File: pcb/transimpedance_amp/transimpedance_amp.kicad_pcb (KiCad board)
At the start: 2 copper layers, 80 x 50 mm, 48 parts, among them P1 CONN_01X05, P2 CONN_01X05, P3 CONN_01X05, P4 CONN_01X05, P5 CONN_01X05, P6 CONN_01X05, P7 CONN_01X05, P8 CONN_01X05, U1 AD8616

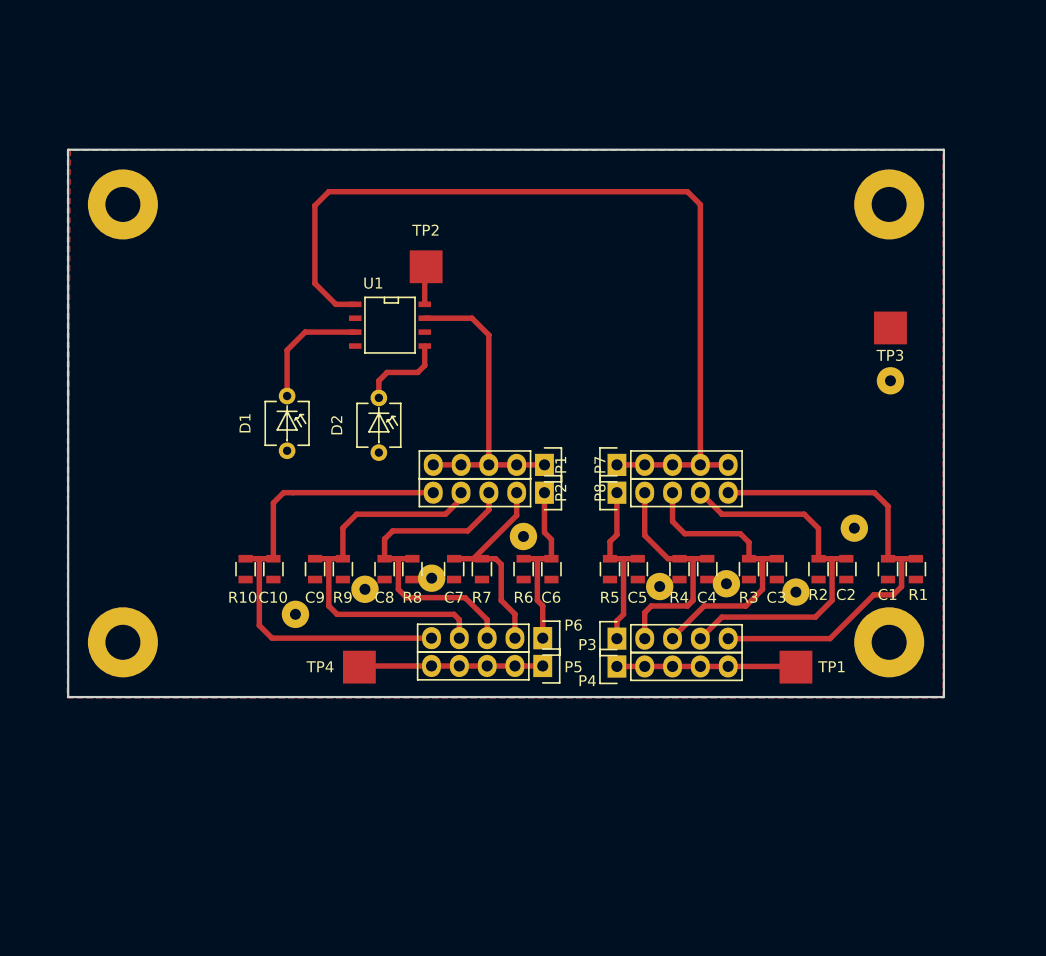
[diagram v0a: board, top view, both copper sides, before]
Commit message: Found a design error. Has to be corrected.
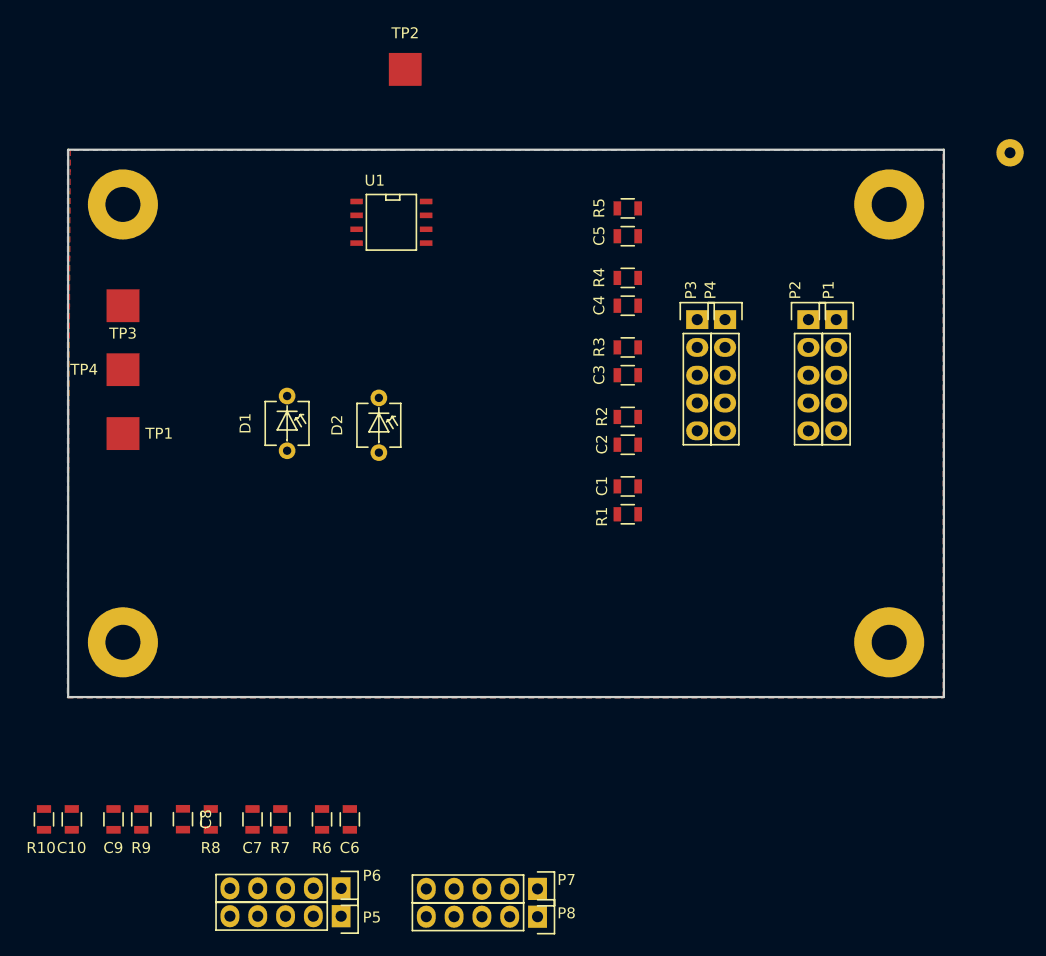
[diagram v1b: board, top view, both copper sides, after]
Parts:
- removed the REF** at (178.8, 115.6)
- removed the REF** at (167.1, 120.7)
- removed the REF** at (173.5, 121.4)
- removed the REF** at (161.0, 120.9)
- removed the REF** at (148.6, 116.3)
- removed the REF** at (140.2, 120.1)
- removed the REF** at (127.8, 123.4)
- removed the REF** at (134.1, 121.2)
- moved TP3 70.1 mm to (112.0, 95.2)
- moved TP1 65.1 mm to (112.0, 106.9)
- moved P7 38.7 mm to (149.9, 148.5)
- moved P8 38.7 mm to (149.9, 151.1)
- moved TP4 34.7 mm to (112.0, 101.1)
- moved P4 33.2 mm to (167.0, 96.5), turned to 0 degrees
- moved R5 33.0 mm to (158.1, 86.4), turned to 180 degrees
- moved C5 30.4 mm to (158.1, 88.9), turned to 180 degrees
- moved P3 30.1 mm to (164.5, 96.5), turned to 0 degrees
- moved C6 29.4 mm to (132.7, 142.2)
- moved C10 29.4 mm to (107.3, 142.2)
- moved C9 29.4 mm to (111.1, 142.2)
- moved C7 29.4 mm to (123.8, 142.2)
- moved P5 29.4 mm to (131.9, 151.0)
- moved R10 29.4 mm to (104.8, 142.2)
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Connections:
- C1 pad 2: GND -> Net-(C1-Pad2)
- C10 pad 2: GND -> Net-(C10-Pad2)
- C2 pad 2: GND -> Net-(C1-Pad2)
- C3 pad 2: GND -> Net-(C1-Pad2)
- C4 pad 2: GND -> Net-(C1-Pad2)
- C5 pad 2: GND -> Net-(C1-Pad2)
- C6 pad 2: GND -> Net-(C10-Pad2)
- C7 pad 2: GND -> Net-(C10-Pad2)
- C8 pad 2: GND -> Net-(C10-Pad2)
- C9 pad 2: GND -> Net-(C10-Pad2)
- D1 pad 1: Net-(D1-Pad1) -> Net-(C1-Pad2)
- D2 pad 1: Net-(D2-Pad1) -> Net-(C10-Pad2)
- R1 pad 2: GND -> Net-(C1-Pad2)
- R10 pad 2: GND -> Net-(C10-Pad2)
- R2 pad 2: GND -> Net-(C1-Pad2)
- R3 pad 2: GND -> Net-(C1-Pad2)
- R4 pad 2: GND -> Net-(C1-Pad2)
- R5 pad 2: GND -> Net-(C1-Pad2)
- R6 pad 2: GND -> Net-(C10-Pad2)
- R7 pad 2: GND -> Net-(C10-Pad2)
- R8 pad 2: GND -> Net-(C10-Pad2)
- R9 pad 2: GND -> Net-(C10-Pad2)
- U1 pad 3: Net-(D1-Pad1) -> Net-(C1-Pad2)
- U1 pad 5: Net-(D2-Pad1) -> Net-(C10-Pad2)
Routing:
- net Net-(P1-Pad1): track 81.7 -> 0.00 mm
- net Net-(C10-Pad1): track 44.9 -> 0.00 mm
- net Net-(C1-Pad1): track 42.8 -> 0.00 mm
- net Net-(C9-Pad1): track 36.3 -> 0.00 mm
- net Net-(C2-Pad1): track 35.1 -> 0.00 mm
- net Net-(C8-Pad1): track 30.5 -> 0.00 mm
- net Net-(P7-Pad1): track 28.5 -> 0.00 mm
- net Net-(C3-Pad1): track 27.5 -> 0.00 mm
- net Net-(C4-Pad1): track 21.6 -> 0.00 mm
- net Net-(C7-Pad1): track 20.2 -> 0.00 mm
- net Net-(C6-Pad1): track 17.0 -> 0.00 mm
- net Net-(P5-Pad1): track 16.8 -> 0.00 mm
- net Net-(C5-Pad1): track 16.4 -> 0.00 mm
- net Net-(P4-Pad1): track 16.4 -> 0.00 mm
- net Net-(D1-Pad1): track 11.1 -> 0.00 mm
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
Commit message: Finished layout. Sill room for optimization.
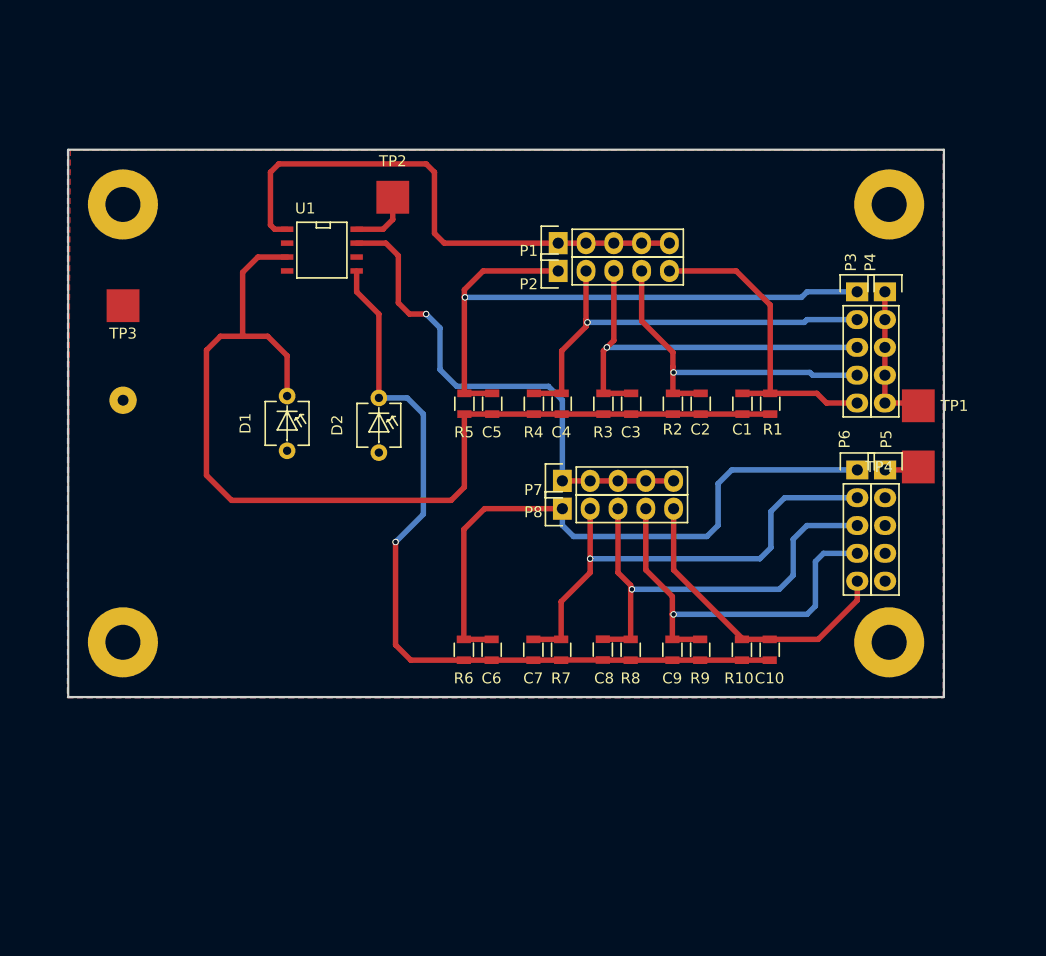
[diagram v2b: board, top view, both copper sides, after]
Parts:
- moved REF** 84.1 mm to (112.0, 103.9)
- moved TP4 73.2 mm to (184.7, 110.0)
- moved TP1 72.7 mm to (184.7, 104.4)
- moved C10 65.6 mm to (171.1, 126.7)
- moved R10 65.6 mm to (168.5, 126.7)
- moved P5 64.3 mm to (181.6, 110.3), turned to 0 degrees
- moved P6 60.7 mm to (179.1, 110.3), turned to 0 degrees
- moved R9 53.4 mm to (164.7, 126.7)
- moved C9 53.4 mm to (162.2, 126.7)
- moved C8 41.4 mm to (155.8, 126.7)
- moved R8 41.4 mm to (158.4, 126.7)
- moved P7 37.3 mm to (152.1, 111.3), turned to 90 degrees
- moved P8 37.3 mm to (152.1, 113.8), turned to 90 degrees
- moved C7 30.0 mm to (149.5, 126.7)
- moved R7 30.0 mm to (152.0, 126.7)
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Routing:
- net Net-(C1-Pad2): track 0.00 -> 93.8 mm
- net Net-(C10-Pad2): track 0.00 -> 74.0 mm, vias 0 -> 1
- net Net-(C5-Pad1): track 0.00 -> 57.5 mm, vias 0 -> 1
- net Net-(C6-Pad1): track 0.00 -> 56.0 mm
- net Net-(P1-Pad1): track 0.00 -> 49.5 mm
- net Net-(P7-Pad1): track 0.00 -> 47.0 mm, vias 0 -> 1
- net Net-(C7-Pad1): track 0.00 -> 44.2 mm, vias 0 -> 1
- net Net-(C8-Pad1): track 0.00 -> 40.2 mm, vias 0 -> 1
- net Net-(C4-Pad1): track 0.00 -> 39.8 mm, vias 0 -> 1
- net Net-(C9-Pad1): track 0.00 -> 37.3 mm, vias 0 -> 1
- net Net-(C3-Pad1): track 0.00 -> 37.0 mm, vias 0 -> 1
- net Net-(C2-Pad1): track 0.00 -> 32.0 mm, vias 0 -> 1
- net Net-(C1-Pad1): track 0.00 -> 29.4 mm
- net Net-(C10-Pad1): track 0.00 -> 28.3 mm
- net Net-(P4-Pad1): track 0.00 -> 13.3 mm
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
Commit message: Finished transimpedance amp. layout. Produced output for v0.1.
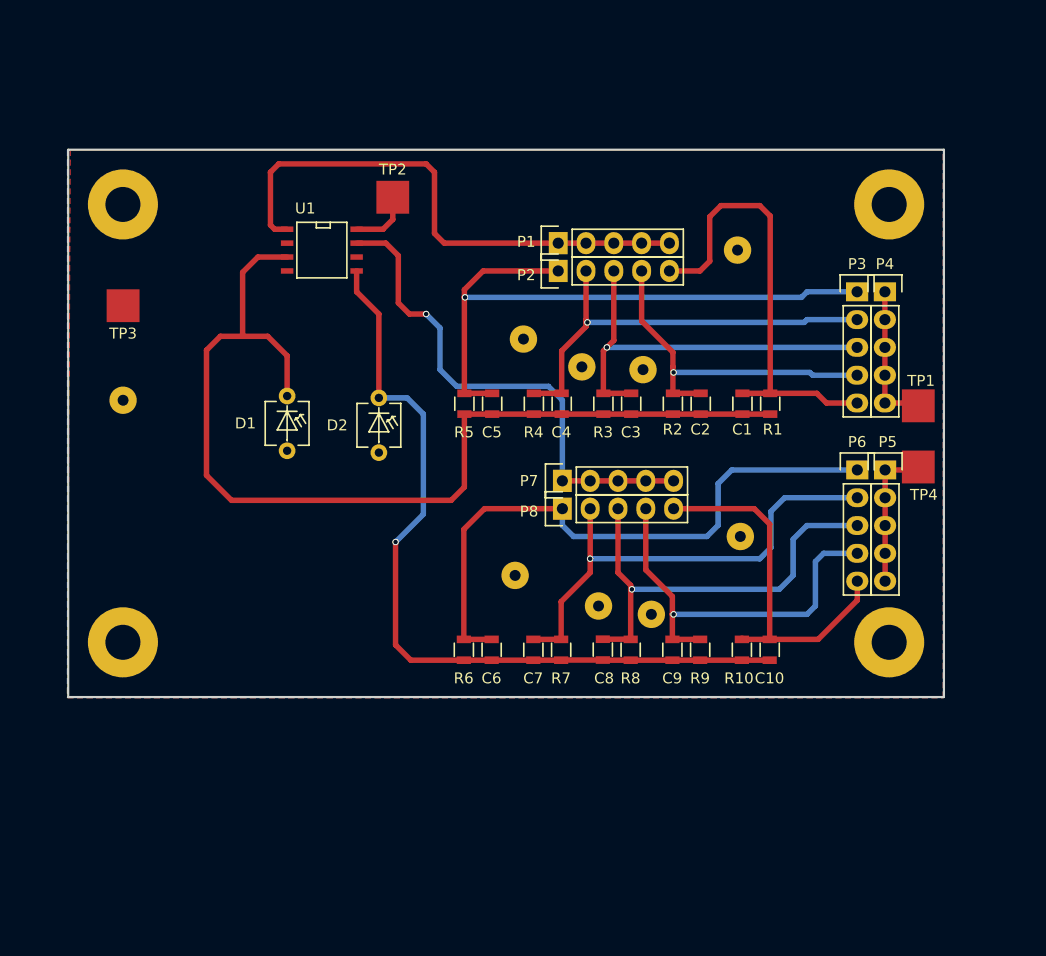
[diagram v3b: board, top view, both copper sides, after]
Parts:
- added REF**: SolderWirePad_single_1mmDrill, Wire_Pads:SolderWirePad_single_1mmDrill, F.Cu at (168.4, 116.3)
- added REF**: SolderWirePad_single_1mmDrill, Wire_Pads:SolderWirePad_single_1mmDrill, F.Cu at (168.1, 90.2)
- added REF**: SolderWirePad_single_1mmDrill, Wire_Pads:SolderWirePad_single_1mmDrill, F.Cu at (153.9, 100.8)
- added REF**: SolderWirePad_single_1mmDrill, Wire_Pads:SolderWirePad_single_1mmDrill, F.Cu at (159.5, 101.1)
- added REF**: SolderWirePad_single_1mmDrill, Wire_Pads:SolderWirePad_single_1mmDrill, F.Cu at (148.6, 98.3)
- added REF**: SolderWirePad_single_1mmDrill, Wire_Pads:SolderWirePad_single_1mmDrill, F.Cu at (160.3, 123.4)
- added REF**: SolderWirePad_single_1mmDrill, Wire_Pads:SolderWirePad_single_1mmDrill, F.Cu at (155.4, 122.7)
- added REF**: SolderWirePad_single_1mmDrill, Wire_Pads:SolderWirePad_single_1mmDrill, F.Cu at (147.8, 119.9)
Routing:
- net Net-(C1-Pad1): track 29.4 -> 41.5 mm
- net Net-(P5-Pad1): track 3.14 -> 13.3 mm
- net Net-(C10-Pad1): track 28.3 -> 33.8 mm
